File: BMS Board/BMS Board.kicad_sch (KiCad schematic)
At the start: 209 parts, among them J1 Conn_01x02, Q1 NMOS, U1 BQ76920PW, U10 TLV70033_SOT23-5, U2 TCA9548APWR, U3 BQ76920PW, U4 BQ76920PW, U5 BQ76920PW, U6 BQ76920PW, U7 BQ76920PW, U8 BQ76920PW, U9 BQ76930DBT

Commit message: Changed Resistance and Capacitance Vals for BQ..30 board
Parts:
- C67, C68, C69, C70, C71, C72, C73, C74, C75, C76: value 220nF -> 1u
- R59, R60, R61, R62, R65, R66, R67, R68, R69: value 100 -> 1000
- U2: value TCA9548APWR -> t
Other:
- note added: "I think according to datasheet RC values for BQ76930 should be typically 1K and min 500 (?)"
- note added: "Nfet rating. VDS- 32V, Current- not much at all, 10A is a lot."
- note added: "Reason for choice of CC as 220nf? Datasheet says typical 1uF"
- note added: "Take the LDO from one of the BQ7692 ICs to the Multiplexer power input, confirm current requirements and put LDO outputs in series as necessary"
- note added: "Try to find alternative for this (!)"

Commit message: used LDO output from BMs to Mux, routed PCB
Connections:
- net 3.3V: no longer R71.1, R72.1, R73.1, R74.1, R75.1, R76.1, R77.1, R78.1, R87.1, U2.24 (VCC)
- net MUX_PWR: now reaches C57.2, U8.8 (REGOUT)
- net MUX_PWR: now also R71.1, R72.1, R73.1, R74.1, R75.1, R76.1, R77.1, R78.1, R87.1, U2.24 (VCC)
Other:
- moved on the sheet: C57
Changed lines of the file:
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@@
 	)
 	(junction
+		(at 367.03 262.89)
+		(diameter 0)
+		(color 0 0 0 0)
+	)
+	(junction
 		(at 140.97 347.98)
 		(diameter 0)
@@
 	)
 	(junction
-		(at 359.41 245.11)
-		(diameter 0)
-		(color 0 0 0 0)
-	)
-	(junction
 		(at 157.48 449.58)
 		(diameter 0)
@@
 	(wire
 		(pts
-			(xy 359.41 245.11) (xy 368.3 245.11)
-		)
-		(stroke
-			(width 0)
-			(type default)
-		)
-	)
-	(wire
-		(pts
 			(xy 223.52 288.29) (xy 219.71 288.29)
 		)
@@
 	(wire
 		(pts
+			(xy 367.03 255.27) (xy 367.03 262.89)
+		)
+		(stroke
+			(width 0)
+			(type default)
+		)
+	)
+	(wire
+		(pts
 			(xy 311.15 269.24) (xy 311.15 273.05)
 		)
@@
 	(wire
 		(pts
-			(xy 368.3 261.62) (xy 368.3 262.89)
+			(xy 374.65 261.62) (xy 374.65 262.89)
 		)
 		(stroke
@@
 	(wire
 		(pts
-			(xy 349.25 245.11) (xy 359.41 245.11)
-		)
-		(stroke
-			(width 0)
-			(type default)
-		)
-	)
-	(wire
-		(pts
 			(xy 241.3 270.51) (xy 252.73 270.51)
 		)
@@
 	(wire
 		(pts
-			(xy 359.41 245.11) (xy 359.41 243.84)
-		)
-		(stroke
-			(width 0)
-			(type default)
-		)
-	)
-	(wire
-		(pts
 			(xy 365.76 194.31) (xy 361.95 194.31)
 		)
@@
 	(wire
 		(pts
-			(xy 361.95 262.89) (xy 368.3 262.89)
+			(xy 361.95 262.89) (xy 367.03 262.89)
 		)
 		(stroke
@@
 	(wire
 		(pts
+			(xy 367.03 262.89) (xy 374.65 262.89)
+		)
+		(stroke
+			(width 0)
+			(type default)
+		)
+	)
+	(wire
+		(pts
 			(xy 265.43 189.23) (xy 261.62 189.23)
 		)
@@
 	(wire
 		(pts
-			(xy 368.3 245.11) (xy 368.3 254)
-		)
-		(stroke
-			(width 0)
-			(type default)
-		)
-	)
-	(wire
-		(pts
 			(xy 363.22 293.37) (xy 363.22 300.99)
 		)
@@
 		)
 	)
-	(label "3.3V"
+	(label "MUX_PWR"
 		(at 382.27 35.56 0)
 		(effects
@@
 		)
 	)
+	(label "MUX_PWR"
+		(at 367.03 255.27 0)
+		(effects
+			(font
+				(size 1.27 1.27)
+			)
+			(justify left bottom)
+		)
+	)
 	(label "THERM6"
 		(at 163.83 283.21 180)
@@
 	(symbol
 		(lib_id "power:GND")
+		(at 374.65 254 180)
+		(unit 1)
+		(body_style 1)
+		(exclude_from_sim no)
+		(in_bom yes)
+		(on_board yes)
+		(in_pos_files yes)
+		(dnp no)
+		(fields_autoplaced yes)
+		(property "Reference" "#PWR063"
+			(at 374.65 247.65 0)
+			(hide yes)
+			(show_name no)
+			(do_not_autoplace no)
+			(effects
+				(font
+					(size 1.27 1.27)
+				)
+			)
+		)
+		(property "Value" "GND"
+			(at 374.65 248.92 0)
+			(show_name no)
+			(do_not_autoplace no)
+			(effects
+				(font
+					(size 1.27 1.27)
+				)
+			)
+		)
+		(property "Footprint" ""
+			(at 374.65 254 0)
+			(hide yes)
+			(show_name no)
+			(do_not_autoplace no)
+			(effects
+				(font
+					(size 1.27 1.27)
+				)
+			)
+		)
+		(property "Datasheet" ""
+			(at 374.65 254 0)
+			(hide yes)
+			(show_name no)
+			(do_not_autoplace no)
+			(effects
+				(font
+					(size 1.27 1.27)
+				)
+			)
+		)
+		(property "Description" "Power symbol creates a global label with name \"GND\" , ground"
+			(at 374.65 254 0)
+			(hide yes)
+			(show_name no)
+			(do_not_autoplace no)
+			(effects
+				(font
+					(size 1.27 1.27)
+				)
+			)
+		)
+		(pin "1"
+		)
+		(instances
+			(project "BMS Board"
+				(path "/a57f7fab-6172-446f-9361-69af31cdb407"
+					(reference "#PWR063")
+					(unit 1)
+				)
+			)
+		)
+	)
+	(symbol
+		(lib_id "power:GND")
 		(at 219.71 77.47 0)
 		(unit 1)
@@
 	(symbol
 		(lib_id "power:GND")
-		(at 359.41 243.84 180)
+		(at 349.25 245.11 180)
 		(unit 1)
 		(body_style 1)
@@
 		(fields_autoplaced yes)
 		(property "Reference" "#PWR044"
-			(at 359.41 237.49 0)
+			(at 349.25 238.76 0)
 			(hide yes)
 			(show_name no)
@@
 		)
 		(property "Value" "GND"
-			(at 359.41 238.76 0)
+			(at 349.25 240.03 0)
 			(show_name no)
 			(do_not_autoplace no)
@@
 		)
 		(property "Footprint" ""
-			(at 359.41 243.84 0)
+			(at 349.25 245.11 0)
 			(hide yes)
 			(show_name no)
@@
 		)
 		(property "Datasheet" ""
-			(at 359.41 243.84 0)
+			(at 349.25 245.11 0)
 			(hide yes)
 			(show_name no)
@@
 		)
 		(property "Description" "Power symbol creates a global label with name \"GND\" , ground"
-			(at 359.41 243.84 0)
+			(at 349.25 245.11 0)
 			(hide yes)
 			(show_name no)
@@
 	(symbol
 		(lib_id "Device:C")
-		(at 368.3 257.81 0)
+		(at 374.65 257.81 0)
 		(unit 1)
 		(body_style 1)
@@
 		(fields_autoplaced yes)
 		(property "Reference" "C57"
-			(at 372.11 256.5399 0)
+			(at 378.46 256.5399 0)
 			(show_name no)
 			(do_not_autoplace no)
@@
 		)
 		(property "Value" "4.7uF"
-			(at 372.11 259.0799 0)
+			(at 378.46 259.0799 0)
 			(show_name no)
 			(do_not_autoplace no)
@@
 		)
 		(property "Footprint" "Capacitor_SMD:C_0603_1608Metric"
-			(at 369.2652 261.62 0)
+			(at 375.6152 261.62 0)
 			(hide yes)
 			(show_name no)
@@
 		)
 		(property "Datasheet" ""
-			(at 368.3 257.81 0)
+			(at 374.65 257.81 0)
 			(hide yes)
 			(show_name no)
@@
 		)
 		(property "Description" "Unpolarized capacitor"
-			(at 368.3 257.81 0)
+			(at 374.65 257.81 0)
 			(hide yes)
 			(show_name no)

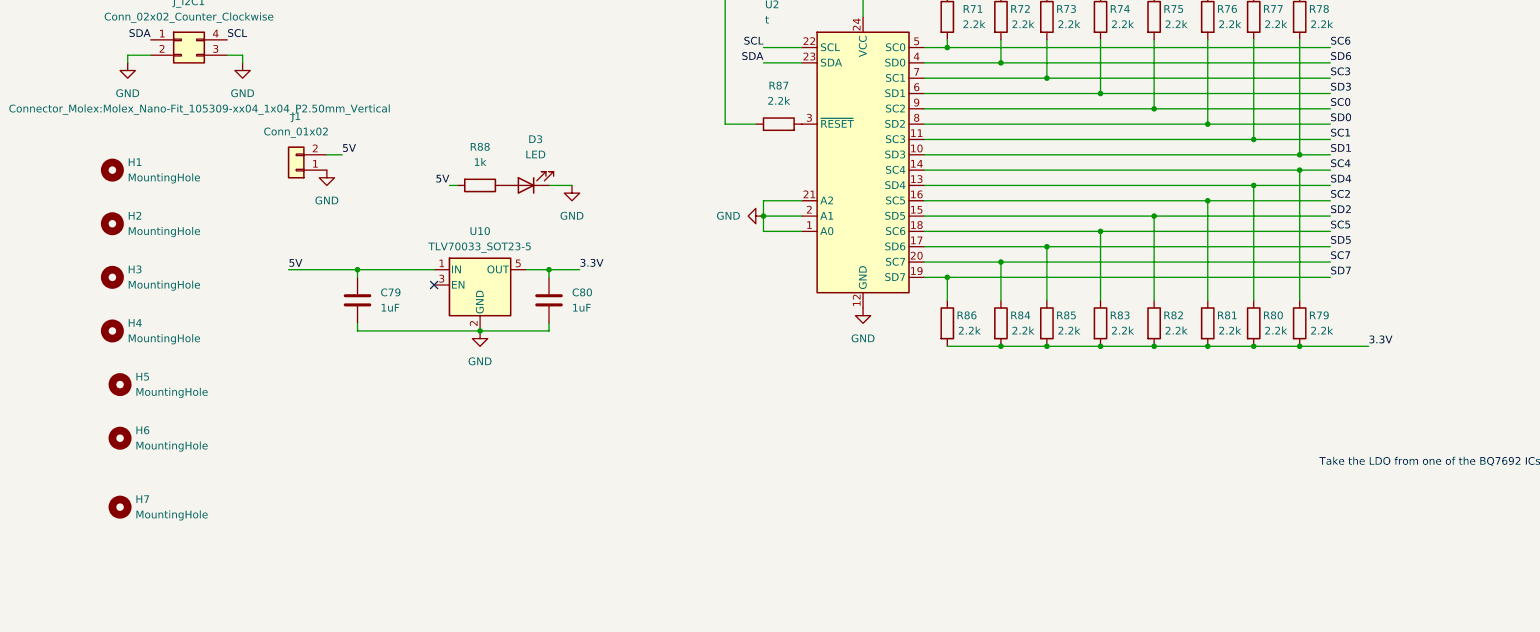
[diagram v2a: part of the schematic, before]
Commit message: small fix on wire label
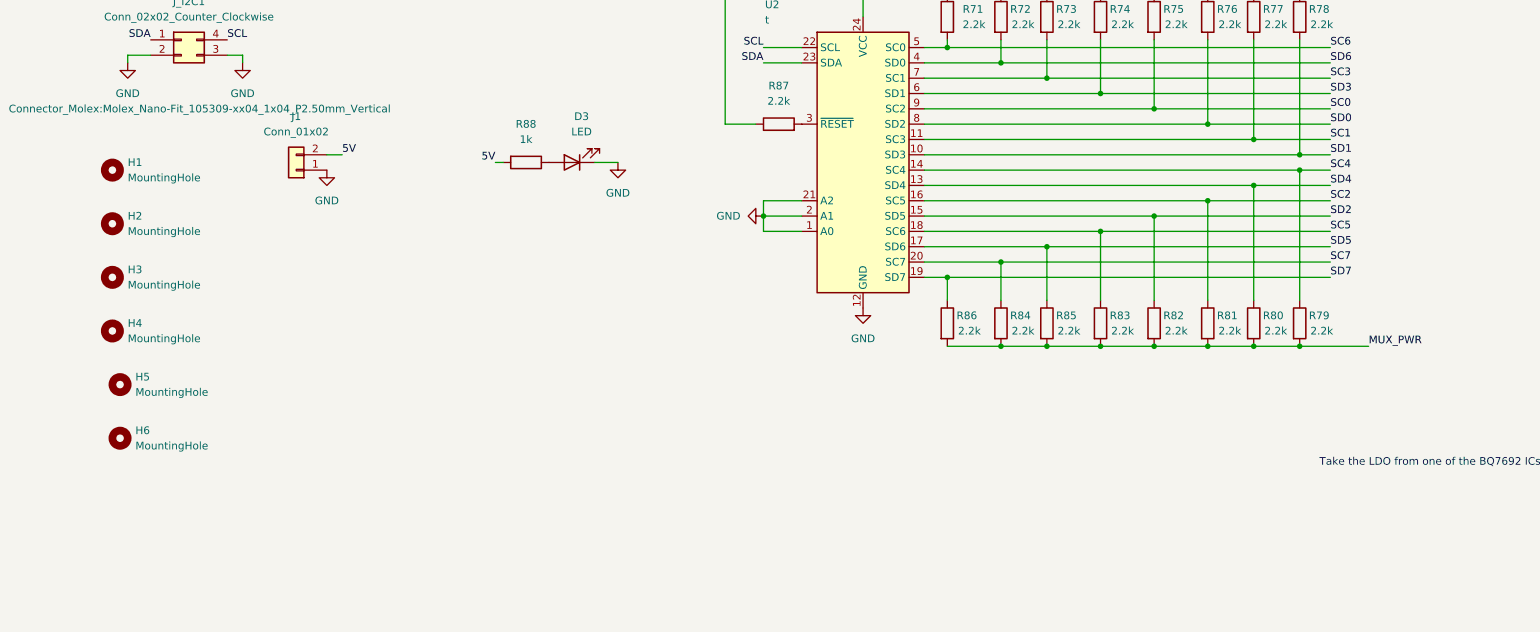
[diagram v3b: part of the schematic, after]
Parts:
- removed C79, C80: 1uF, Capacitor_SMD:C_0603_1608Metric, symbol Device:C
- removed H7: MountingHole, MountingHole:MountingHole_3.2mm_M3_DIN965, symbol Mechanical:MountingHole
- removed U10: TLV70033_SOT23-5, Package_TO_SOT_SMD:SOT-23-5, symbol Regulator_Linear:TLV70033_SOT23-5
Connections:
- net 3.3V is gone; now on net MUX_PWR: R79.2, R80.2, R81.2, R82.2, R83.2, R84.2, R85.2, R86.2
- no-connect marks 17 -> 16
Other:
- moved on the sheet: D3, R88
